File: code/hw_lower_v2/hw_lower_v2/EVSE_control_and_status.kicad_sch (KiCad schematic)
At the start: 17 parts, among them U3 DRV8220DRL, U4 TLV1805

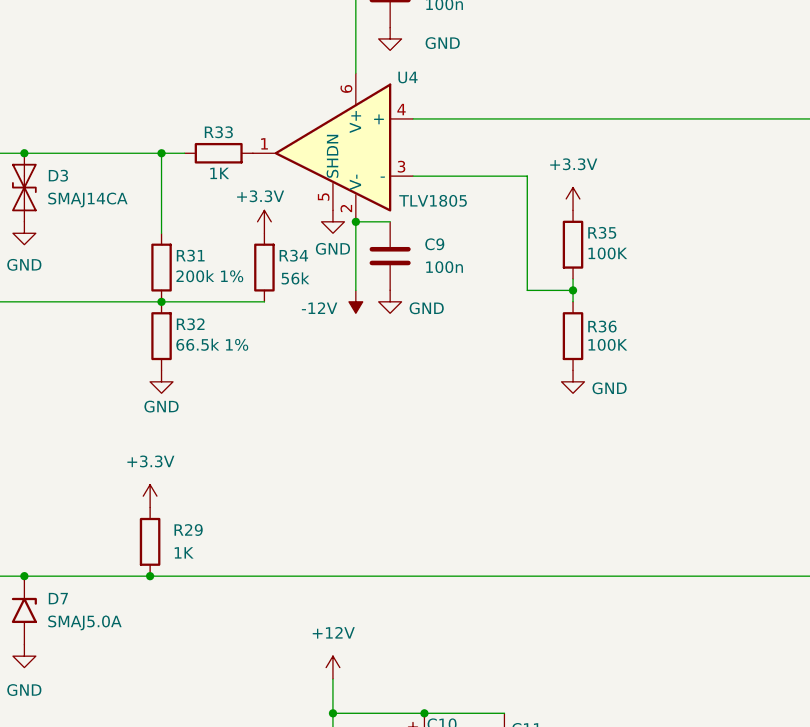
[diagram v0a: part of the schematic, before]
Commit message: simplify component values
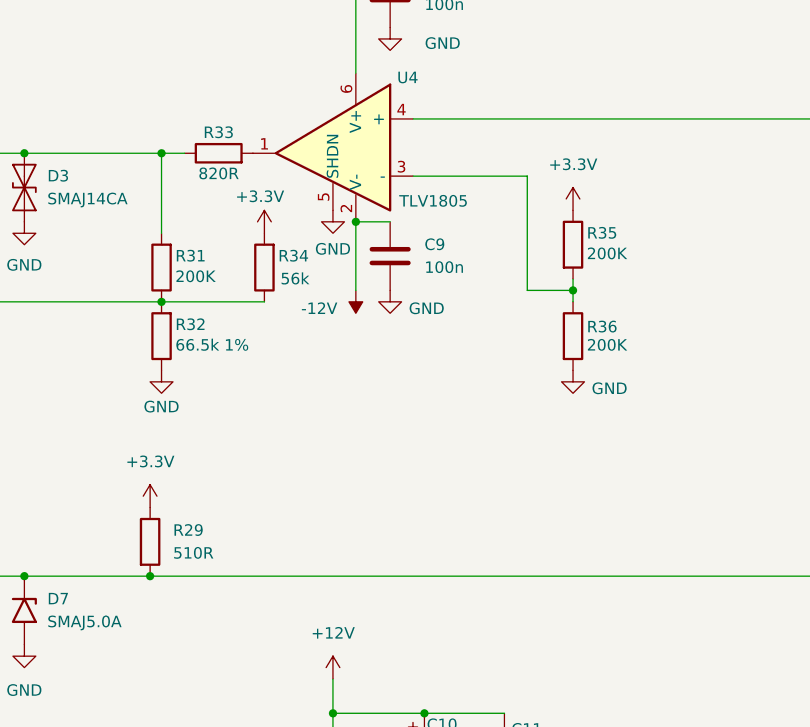
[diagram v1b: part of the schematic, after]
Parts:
- C11, C8, C9: LCSC C38141 -> C327162
- R29: value 1K -> 510R; LCSC C21190 -> C23193
- R31: value 200k 1% -> 200K
- R33: value 1K -> 820R; LCSC C21190 -> C23253
- R35, R36: value 100K -> 200K; LCSC C25803 -> C2989567
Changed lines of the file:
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@@
+		(effects
+			(font
+				(face "FreeMono")
+				(size 1.27 1.27)
+			)
+			(justify left)
+		)
+	)
+	(hierarchical_label "LOCK_SENSE_OUT"
+		(shape input)
+		(at 46.99 156.21 180)
+		(fields_autoplaced yes)
 		(effects
 			(font
 				(size 1.27 1.27)
 			)
-			(justify left)
-		)
-	)
-	(hierarchical_label "LOCK_SENSE_OUT"
+			(justify right)
+		)
+	)
+	(hierarchical_label "CONTROL_PILOT_OUT"
 		(shape input)
-		(at 46.99 156.21 180)
+		(at 48.26 43.18 180)
 		(fields_autoplaced yes)
 		(effects
@@
 		)
 	)
-	(hierarchical_label "CONTROL_PILOT_OUT"
+	(hierarchical_label "PROXIMITY_PILOT"
 		(shape input)
-		(at 48.26 43.18 180)
+		(at 48.26 90.17 180)
 		(fields_autoplaced yes)
 		(effects
@@
 		)
 	)
-	(hierarchical_label "PROXIMITY_PILOT"
+	(hierarchical_label "CONTROL_PILOT_PWM"
 		(shape input)
-		(at 48.26 90.17 180)
+		(at 149.86 39.37 0)
 		(fields_autoplaced yes)
 		(effects
@@
 				(size 1.27 1.27)
 			)
-			(justify right)
-		)
-	)
-	(hierarchical_label "CONTROL_PILOT_PWM"
+			(justify left)
+		)
+	)
+	(hierarchical_label "LOCK_B_OUT"
 		(shape input)
-		(at 149.86 39.37 0)
+		(at 48.26 132.08 180)
 		(fields_autoplaced yes)
 		(effects
@@
 				(size 1.27 1.27)
 			)
-			(justify left)
-		)
-	)
-	(hierarchical_label "LOCK_B_OUT"
+			(justify right)
+		)
+	)
+	(hierarchical_label "LOCK_A"
 		(shape input)
-		(at 48.26 132.08 180)
+		(at 149.86 121.92 0)
 		(fields_autoplaced yes)
 		(effects
@@
 				(size 1.27 1.27)
 			)
-			(justify right)
-		)
-	)
-	(hierarchical_label "LOCK_A"
+			(justify left)
+		)
+	)
+	(hierarchical_label "LOCK_SENSE"
 		(shape input)
-		(at 149.86 121.92 0)
+		(at 149.86 156.21 0)
 		(fields_autoplaced yes)
 		(effects
@@
 		)
 	)
-	(hierarchical_label "LOCK_SENSE"
+	(hierarchical_label "LOCK_SENSE_GND"
 		(shape input)
-		(at 149.86 156.21 0)
+		(at 46.99 171.45 180)
 		(fields_autoplaced yes)
 		(effects
@@
 				(size 1.27 1.27)
 			)
-			(justify left)
-		)
-	)
-	(hierarchical_label "LOCK_SENSE_GND"
+			(justify right)
+		)
+	)
+	(hierarchical_label "CONTROL_PILOT_SENSE"
 		(shape input)
-		(at 46.99 171.45 180)
+		(at 48.26 59.69 180)
 		(fields_autoplaced yes)
 		(effects
@@
 		)
 	)
-	(hierarchical_label "CONTROL_PILOT_SENSE"
+	(hierarchical_label "PROXIMITY_PILOT_SENSE"
 		(shape input)
-		(at 48.26 59.69 180)
+		(at 149.86 90.17 0)
 		(fields_autoplaced yes)
 		(effects
@@
 				(size 1.27 1.27)
 			)
-			(justify right)
-		)
-	)
-	(hierarchical_label "PROXIMITY_PILOT_SENSE"
+			(justify left)
+		)
+	)
+	(hierarchical_label "LOCK_B"
 		(shape input)
-		(at 149.86 90.17 0)
+		(at 149.86 127 0)
 		(fields_autoplaced yes)
 		(effects
@@
 		)
 	)
-	(hierarchical_label "LOCK_B"
+	(hierarchical_label "LOCK_A_OUT"
 		(shape input)
-		(at 149.86 127 0)
+		(at 48.26 116.84 180)
 		(fields_autoplaced yes)
 		(effects
@@
 				(size 1.27 1.27)
 			)
-			(justify left)
-		)
-	)
-	(hierarchical_label "LOCK_A_OUT"
-		(shape input)
-		(at 48.26 116.84 180)
-		(fields_autoplaced yes)
-		(effects
-			(font
-				(size 1.27 1.27)
-			)
 			(justify right)
 		)
@@
 			)
 		)
-		(property "Value" "1K"
+		(property "Value" "820R"
 			(at 82.55 45.466 90)
 			(effects
@@
 			)
 		)
-		(property "LCSC" "C21190"
+		(property "LCSC" "C23253"
 			(at 82.55 43.18 0)
 			(effects
@@
 			)
 		)
-		(property "Value" "100K"
+		(property "Value" "200K"
 			(at 123.444 54.356 0)
 			(effects
@@
 			)
 		)
-		(property "LCSC" "C25803"
+		(property "LCSC" "C2989567"
 			(at 121.92 53.34 0)
 			(effects
@@
 			)
 		)
-		(property "Value" "100K"
+		(property "Value" "200K"
 			(at 123.444 64.516 0)
 			(effects
@@
 			)
 		)
-		(property "LCSC" "C25803"
+		(property "LCSC" "C2989567"
 			(at 121.92 63.5 0)
 			(effects
@@
 			)
 		)
-		(property "LCSC" "C38141"
+		(property "LCSC" "C327162"
 			(at 101.6 54.61 0)
 			(effects
@@
 			)
 		)
-		(property "LCSC" "C38141"
+		(property "LCSC" "C327162"
 			(at 101.6 25.4 0)
 			(effects
@@
 			)
 		)
-		(property "Value" "1K"
+		(property "Value" "510R"
 			(at 77.47 87.6299 0)
 			(effects
@@
 			)
 		)
-		(property "LCSC" "C21190"
+		(property "LCSC" "C23193"
 			(at 74.93 86.36 0)
 			(effects
@@
 			)
 		)
-		(property "Value" "200k 1%"
+		(property "Value" "200K"
 			(at 77.724 56.896 0)
 			(effects
@@
 			)
 		)
-		(property "LCSC" "C38141"
+		(property "LCSC" "C327162"
 			(at 114.3 109.22 0)
 			(effects

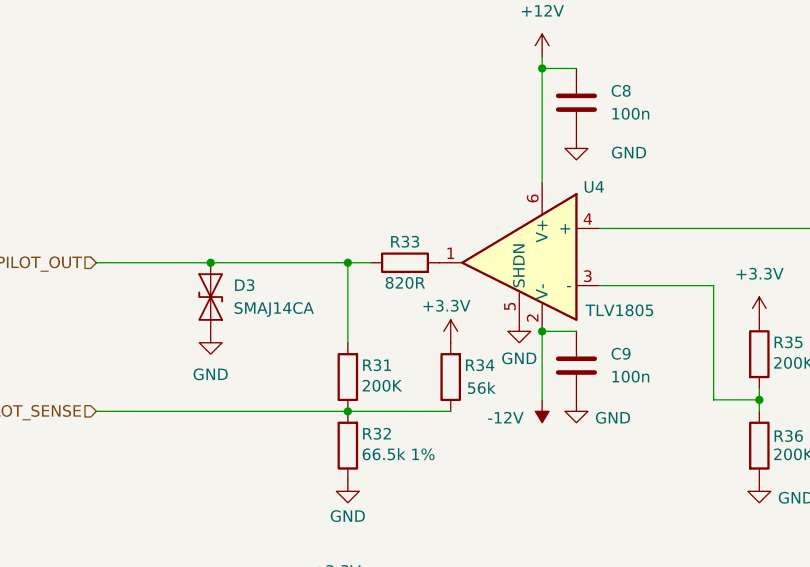
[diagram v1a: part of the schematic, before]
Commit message: add JLCPCB tooling holes and simplify further
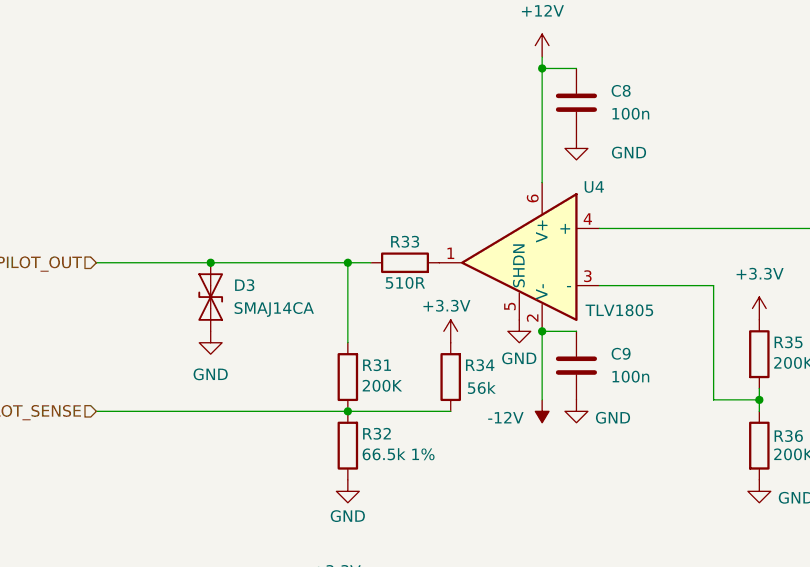
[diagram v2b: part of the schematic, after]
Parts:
- R33: value 820R -> 510R; LCSC C23253 -> C23193
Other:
- title: EVSE -> BlueEVSE
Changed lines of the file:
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@@
 	(paper "A4")
 	(title_block
-		(title "EVSE")
+		(title "BlueEVSE")
 		(date "2024-07-14")
 		(rev "V2")
@@
 			)
 		)
-		(property "Value" "820R"
+		(property "Value" "510R"
 			(at 82.55 45.466 90)
 			(effects
@@
 			)
 		)
-		(property "LCSC" "C23253"
+		(property "LCSC" "C23193"
 			(at 82.55 43.18 0)
 			(effects

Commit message: wip
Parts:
- added R38: 510R, Resistor_SMD:R_0603_1608Metric, symbol Device:R
- added R39: 20k, Resistor_SMD:R_0603_1608Metric, symbol Device:R
- C10: LCSC C72485 -> C86602
- R32: value 66.5k 1% -> 20k; LCSC C861515 -> (none)
- R33: value 510R -> 1K; LCSC C23193 -> (none)
- R34: value 56k -> 20k; LCSC C5250755 -> (none)
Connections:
- net +3.3V: now also R34.1; no longer R34.2
- net -12V: now also U4.5 (SHDN)
- net CONTROL_PILOT_SENSE: now also R39.2; no longer R34.1
- net GND: now also R38.2; no longer U4.5 (SHDN)
- net PROXIMITY_PILOT: now also R38.1
- new net: R34.2, R39.1
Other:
- note added: "Rpp 100ohm -> Vout 0.46V Rpp 1500ohm -> Vout 1.41V"
- moved on the sheet: D2, D3, D7, R29, R30, R31, R32, R35, R36
